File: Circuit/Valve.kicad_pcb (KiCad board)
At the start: 2 copper layers, 95 x 72.1 mm, 24 parts, among them CN1 GROVE, CN2 Conn_01x04_Male, CN3 ST-LINK, CN4 TTL-232R-3V3, SW1 RESET, U1 STM32L010F4P6

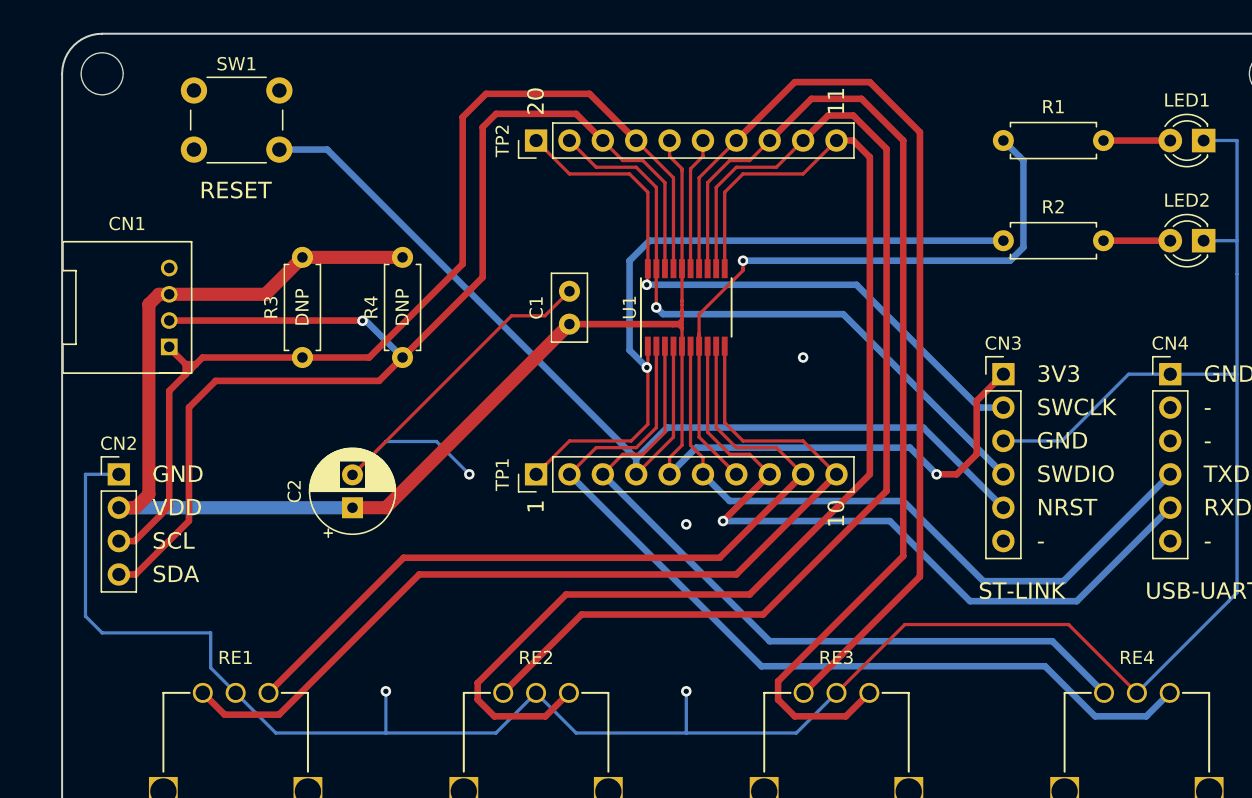
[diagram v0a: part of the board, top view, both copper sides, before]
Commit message: 斜め配線を削減して水平垂直配線に変換
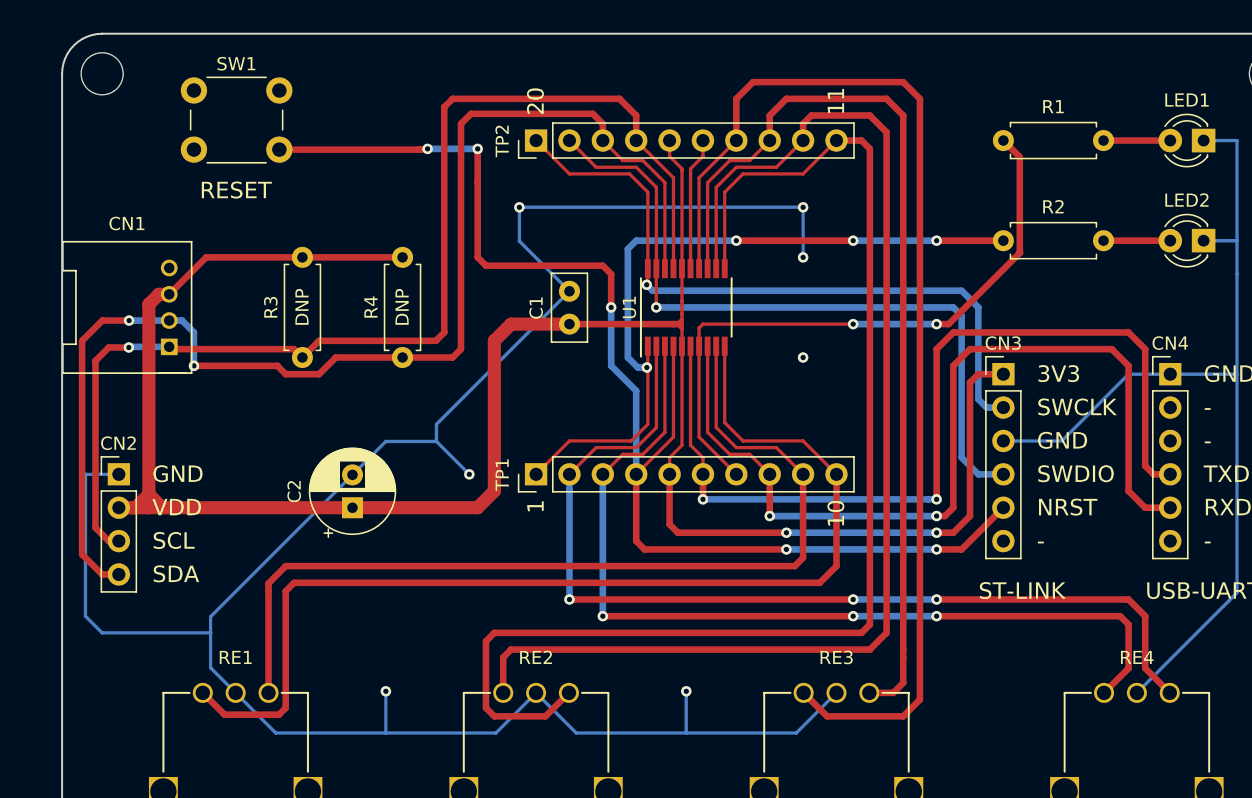
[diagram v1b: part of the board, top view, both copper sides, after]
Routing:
- net VDD: track 147.4 -> 164.3 mm, vias 1 -> 2
- net TXD: track 52.4 -> 69.2 mm, vias 0 -> 2
- net GND: track 226.6 -> 242.6 mm, vias 5 -> 7
- net NRST: track 80.5 -> 95.7 mm, vias 0 -> 5
- net /PC15: track 57.6 -> 69.6 mm, vias 0 -> 3
- net RXD: track 57.1 -> 68.4 mm, vias 1 -> 2
- net /PB1: track 74.6 -> 85.0 mm
- net /PA6: track 84.0 -> 93.4 mm
- net /PA4: track 72.4 -> 81.7 mm
- net /PA3: track 61.8 -> 70.4 mm
- net /PA7: track 80.1 -> 71.8 mm
- net /PA5: track 89.0 -> 97.1 mm
- net SCL: track 81.5 -> 88.4 mm, vias 0 -> 1
- net /PC14: track 68.3 -> 74.8 mm, vias 0 -> 3
- net SWDIO: track 48.9 -> 55.2 mm
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
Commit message: SWD に GND ガードを追加
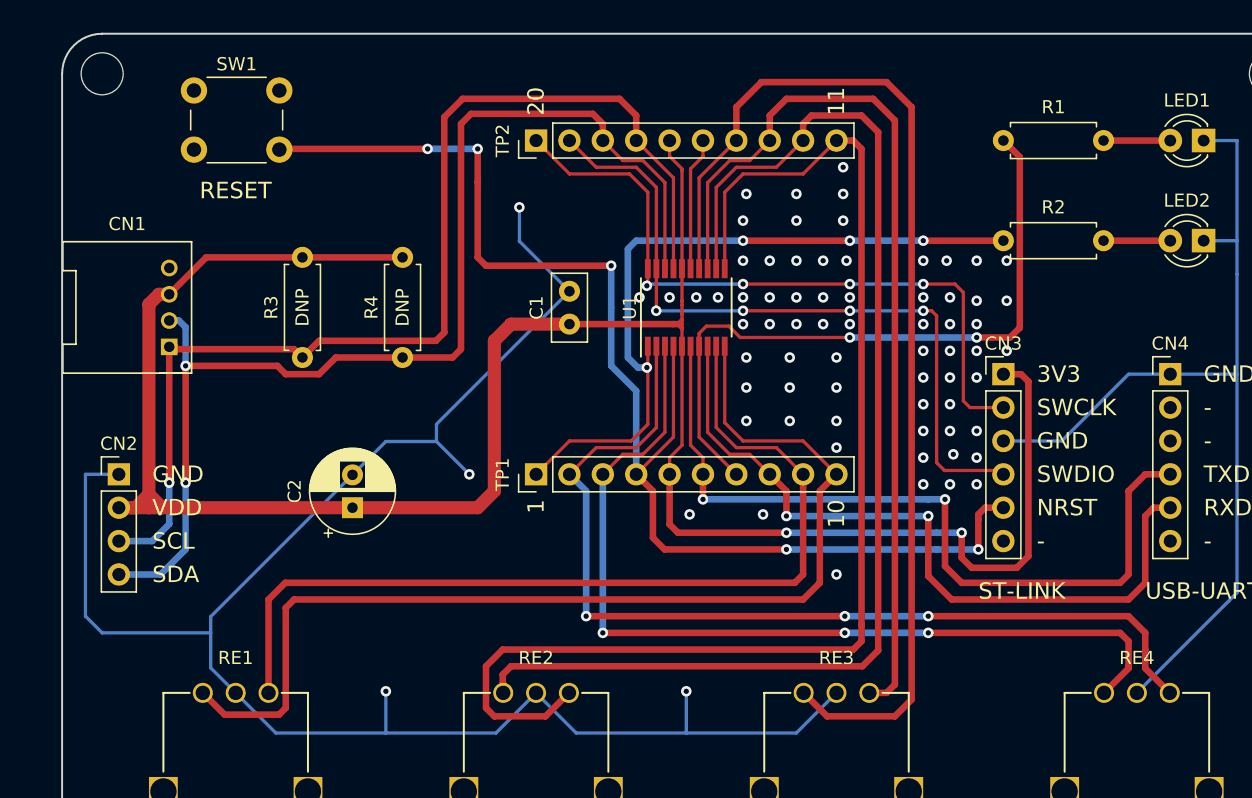
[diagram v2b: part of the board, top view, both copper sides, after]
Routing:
- net GND: track 242.6 -> 217.2 mm, vias 7 -> 72
- net RXD: track 68.4 -> 56.7 mm
- net VDD: track 164.3 -> 173.3 mm
- net TXD: track 69.2 -> 60.4 mm
- net SDA: track 95.6 -> 88.7 mm
- net /PA1: track 48.2 -> 52.0 mm
- net SCL: track 88.4 -> 84.8 mm
- net /PB1: track 85.0 -> 82.9 mm
- net /PA5: track 97.1 -> 95.4 mm
- net /PA7: track 71.8 -> 70.4 mm
- net /PA6: track 93.4 -> 92.2 mm
- net NRST: track 95.7 -> 96.7 mm
- net SWCLK: track 52.3 -> 53.2 mm, vias 1 -> 4
- net /PC14: track 74.8 -> 74.0 mm
- net /PA4: track 81.7 -> 81.0 mm
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
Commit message: R1 用配線を SWD の上側を通すように修正
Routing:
- net /PA1: track 52.0 -> 50.3 mm
- net GND: vias 72 -> 77

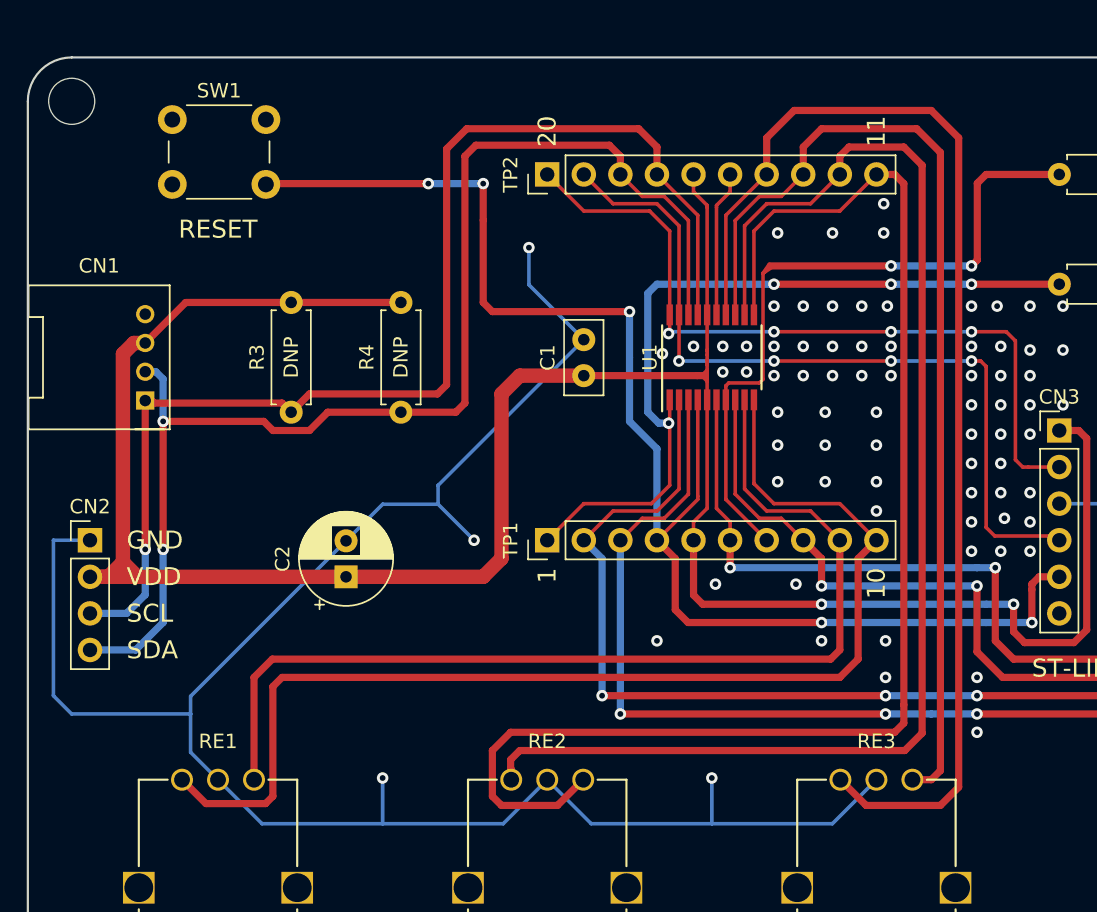
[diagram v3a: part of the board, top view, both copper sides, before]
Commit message: I2C に GND ガードを追加
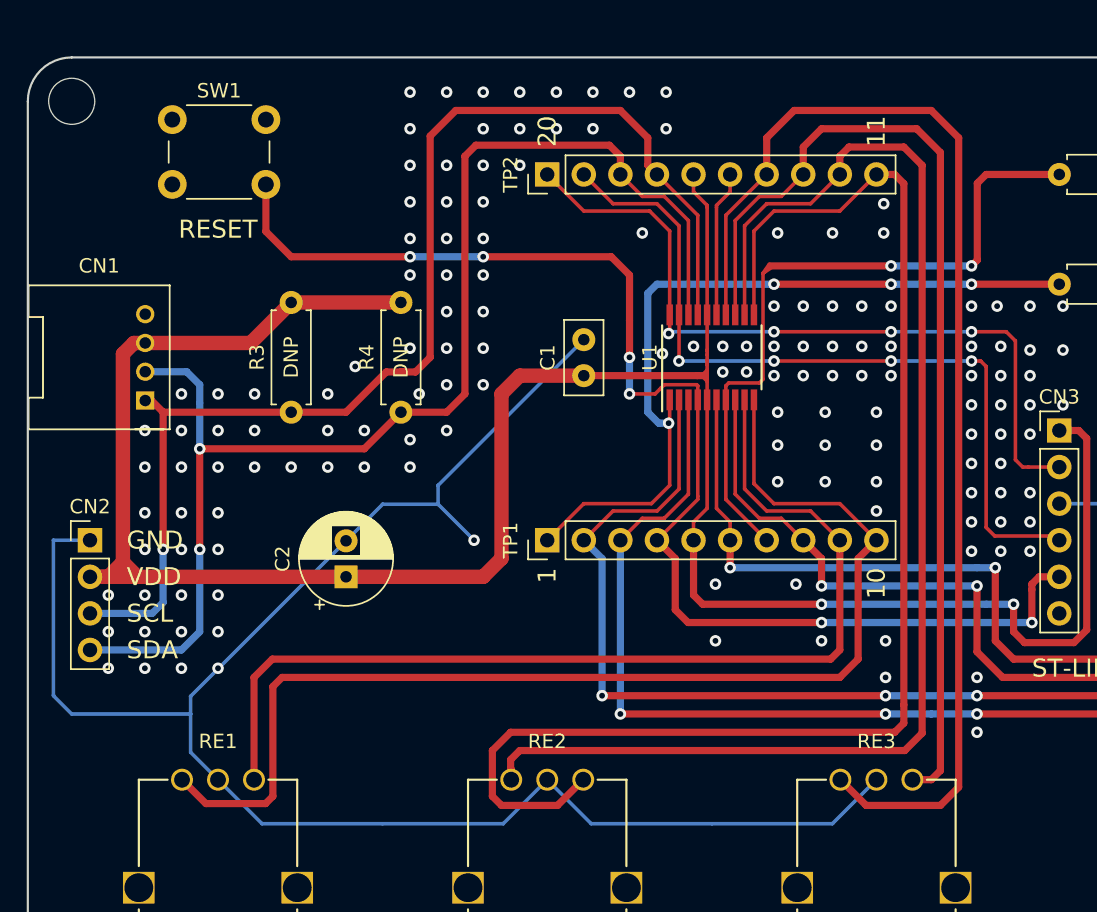
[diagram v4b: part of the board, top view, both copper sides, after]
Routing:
- net GND: track 217.2 -> 202.9 mm, vias 77 -> 149
- net NRST: track 96.7 -> 90.2 mm, vias 5 -> 6
- net SDA: track 88.7 -> 91.3 mm
- net SCL: track 84.8 -> 86.5 mm

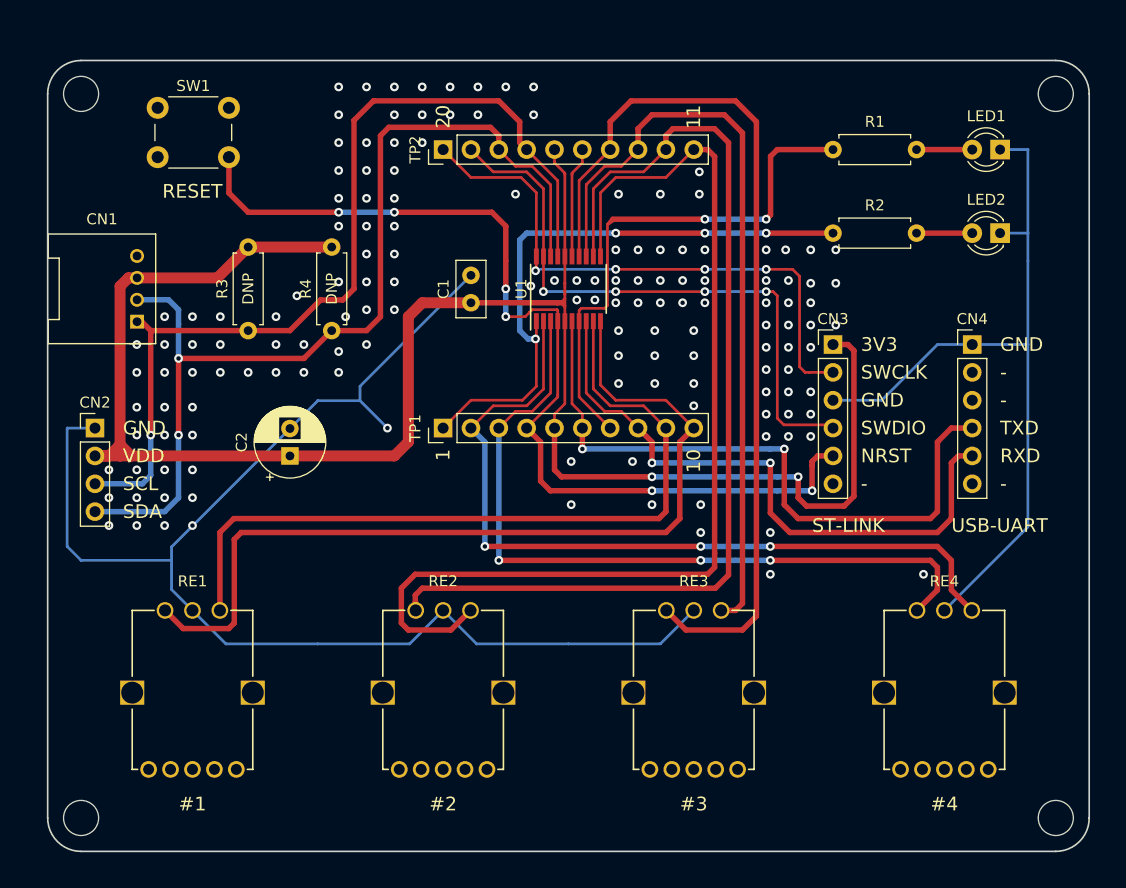
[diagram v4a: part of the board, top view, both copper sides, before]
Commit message: GND ビア打ちとティアドロップ設定
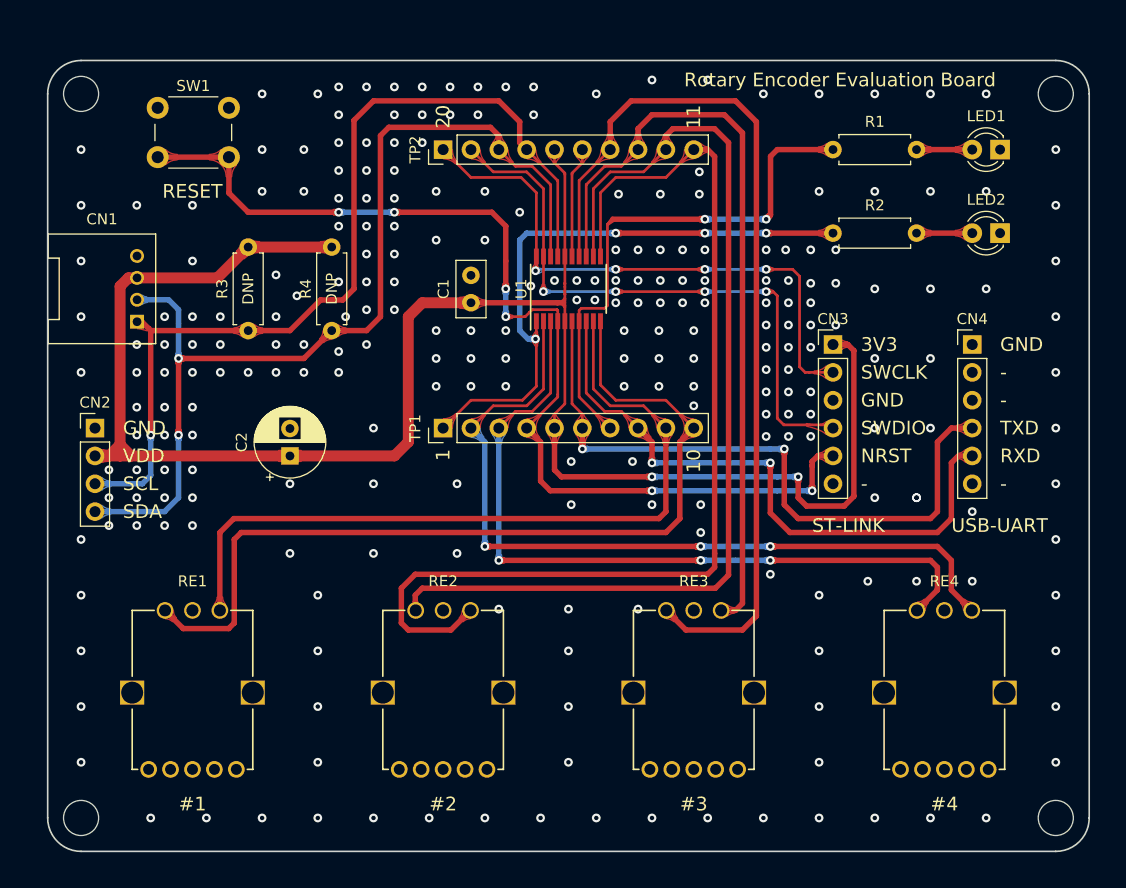
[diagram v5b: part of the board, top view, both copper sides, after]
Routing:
- net GND: track 202.9 -> 10.1 mm, vias 149 -> 254
- net NRST: track 90.2 -> 96.7 mm
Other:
- board text added: "Rotary Encoder Evaluation Board"
